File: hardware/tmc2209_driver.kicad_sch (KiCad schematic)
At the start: 10 parts

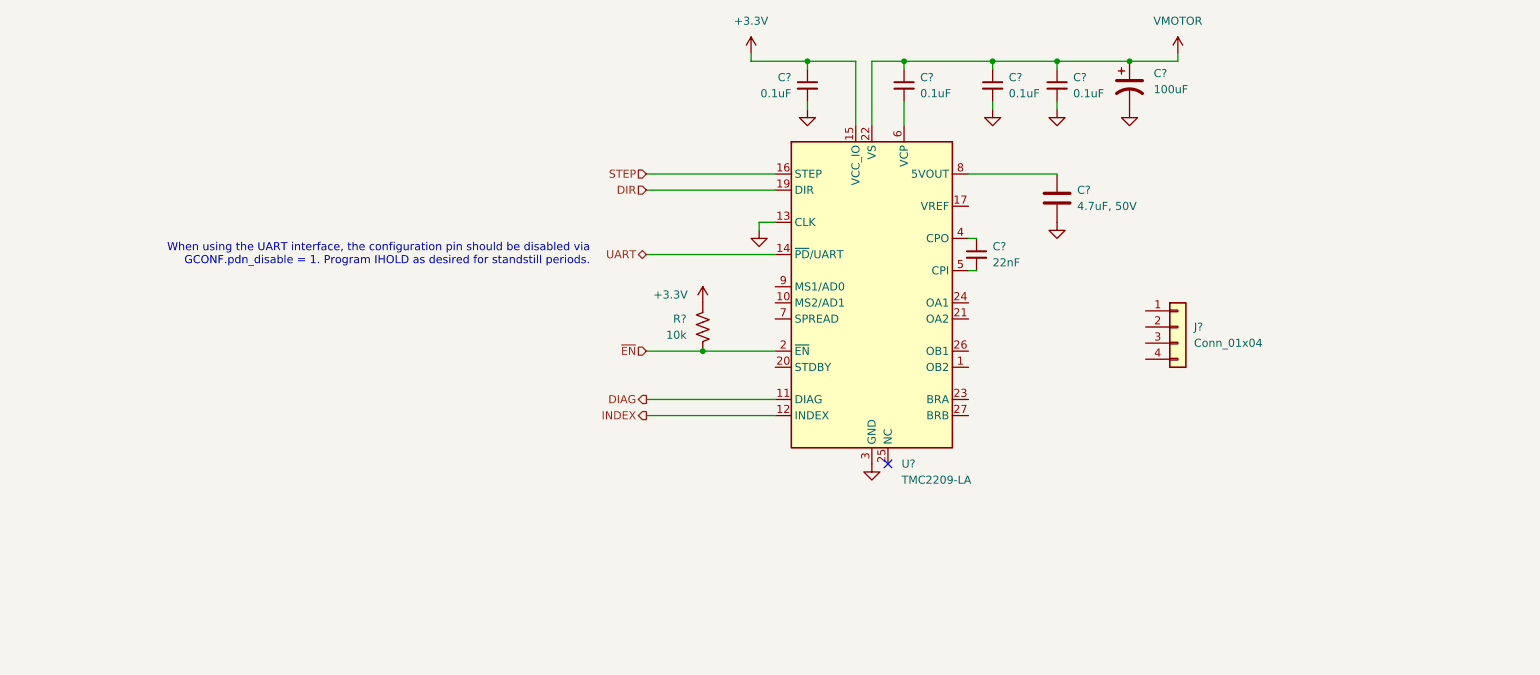
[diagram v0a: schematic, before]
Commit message: TMC2209 Schematic Improvements
Sense resistors and status LEDs
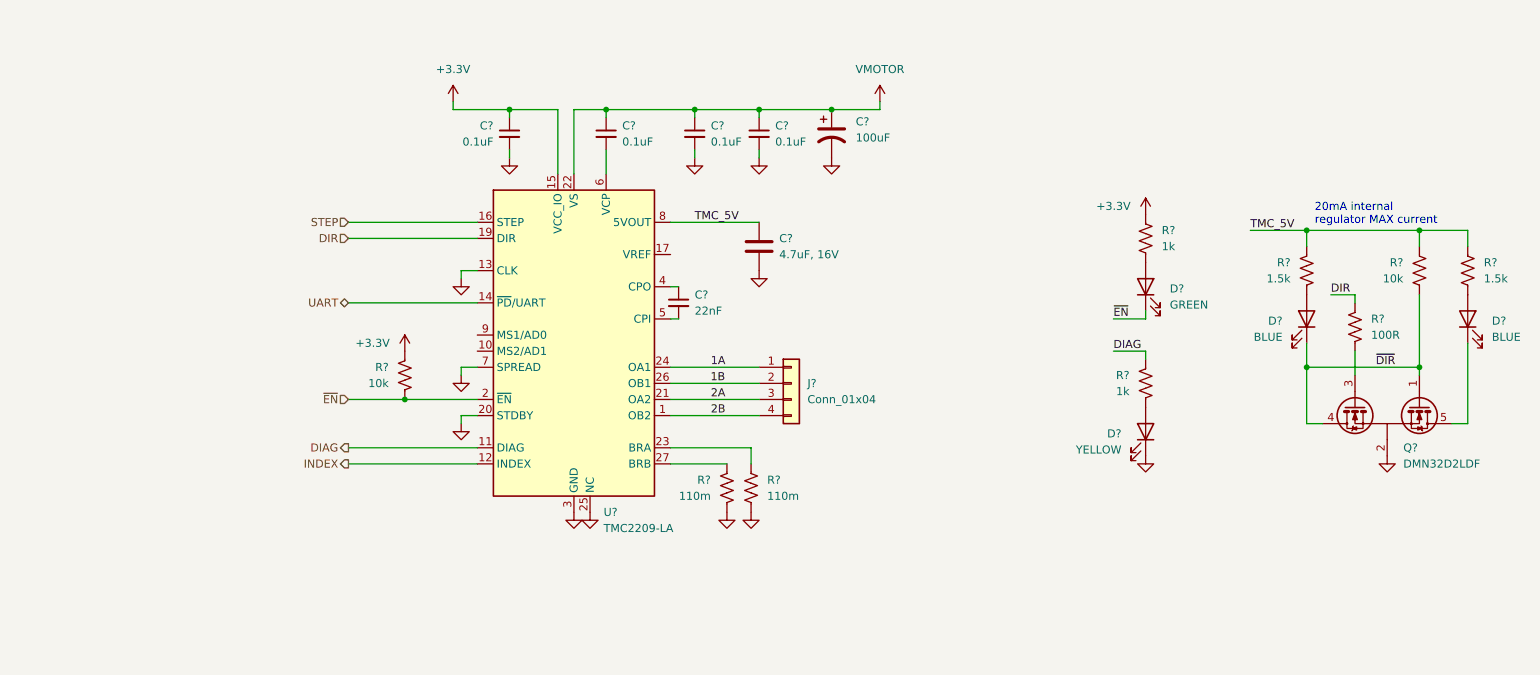
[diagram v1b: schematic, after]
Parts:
- removed C?: 4.7uF, 50V, Capacitor_SMD:C_1206_3216Metric_Pad1.33x1.80mm_HandSolder, symbol Device:C
- added C?: 4.7uF, 16V, Capacitor_SMD:C_0805_2012Metric, symbol Device:C
- added D? (x2): BLUE, Diode_SMD:D_0805_2012Metric, symbol Device:LED
- added D?: YELLOW, Diode_SMD:D_0805_2012Metric, symbol Device:LED
- added D?: GREEN, Diode_SMD:D_0805_2012Metric, symbol Device:LED
- added Q?: DMN32D2LDF, Package_TO_SOT_SMD:SOT-353_SC-70-5, symbol Transistor_FET:DMN32D2LDF
- added R? (x2): 1k, Resistor_SMD:R_0603_1608Metric, symbol Device:R_US
- added R? (x2): 1.5k, Resistor_SMD:R_0603_1608Metric, symbol Device:R_US
- added R? (x2): 110m, Resistor_SMD:R_2512_6332Metric, symbol Device:R_US
- added R?: 10k, Resistor_SMD:R_0603_1608Metric, symbol Device:R_US
- added R?: 100R, Resistor_SMD:R_0603_1608Metric, symbol Device:R_US
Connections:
- net +3.3V: now also R?.1
- net DIAG: now also R?.1
- net DIR: now also R?.1
- net GND: now also U?.20 (STDBY), U?.25 (NC), U?.7 (SPREAD), C?.2, D?.1 (K), Q?.2 (S), R?.1, R?.1
- net ~{EN}: now also D?.1 (K)
- net 2B: now reaches U?.1 (OB2)
- net 2B: now also J?.4 (Pin_4)
- net 2A: now reaches U?.21 (OA2)
- net 2A: now also J?.3 (Pin_3)
- net at U?.23 (BRA): now also R?.2
- net 1A: now reaches U?.24 (OA1)
- net 1A: now also J?.1 (Pin_1)
- net 1B: now reaches U?.26 (OB1)
- net 1B: now also J?.2 (Pin_2)
- net at U?.27 (BRB): now also R?.2
- net TMC_5V: now reaches U?.8 (5VOUT)
- net TMC_5V: now also C?.1, R?.1, R?.1, R?.1
- new net: D?.2 (A), R?.2 (x4)
- new net: D?.1 (K), Q?.5 (D1)
- new net: Q?.3 (G2), R?.2
- new net ~{DIR}: D?.1 (K), Q?.1 (G1), Q?.4 (D2), R?.2
- no-connect marks 1 -> 0
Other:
- note added: "20mA internal regulator MAX current"
- note removed: "When using the UART interface, the configuration pin should be disabled via GCONF.pdn_disable = 1. Program IHOLD as desired for standstill periods."
- moved on the sheet: C?, J?, R?, U?

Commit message: Random changes & LED additions
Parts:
- added Q?: AO3400A, Package_TO_SOT_SMD:SOT-23, symbol Transistor_FET:AO3400A
- added R?: 100R, Resistor_SMD:R_0603_1608Metric, symbol Device:R_US
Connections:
- net +3.3V: now also R?.1
- net DIAG: now also R?.1; no longer R?.1
- net GND: now also Q?.2 (S); no longer D?.1 (K)
- new net: Q?.1 (G), R?.2
- new net: D?.1 (K), Q?.3 (D)
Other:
- note added: "Connect to interrupt-capable GPIO for sensorless homing."
- note added: "DETERMINE NEED OF PULL UP/DOWN RESISTORS ON DIR AND DIAG"
- moved on the sheet: D?, Q?, R?

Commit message: Connector Updates
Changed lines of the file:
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@@
 	(text "DETERMINE NEED OF PULL UP/DOWN\nRESISTORS ON DIR AND DIAG"
 		(exclude_from_sim no)
-		(at 199.39 152.4 0)
+		(at 196.85 152.4 0)
 		(effects
 			(font

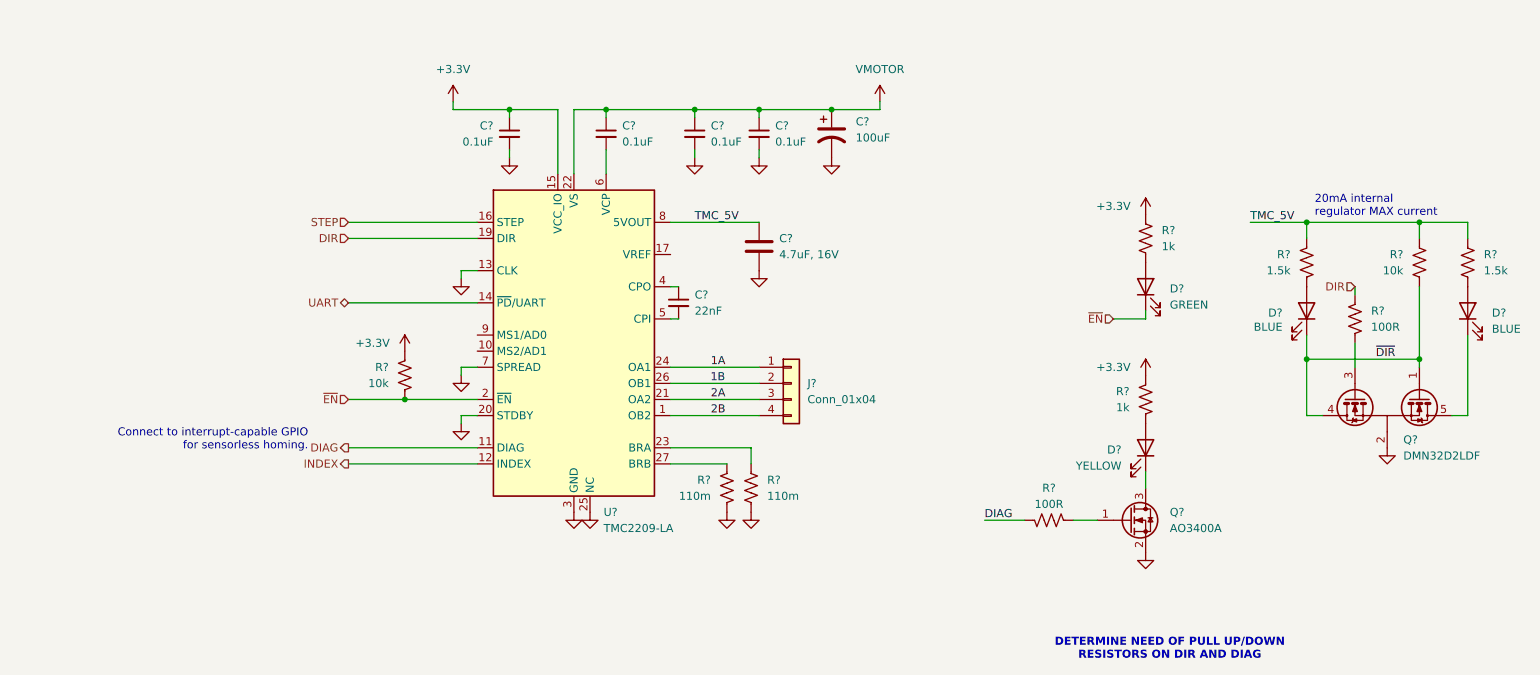
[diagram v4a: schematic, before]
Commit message: Complete TMC2209 sheet
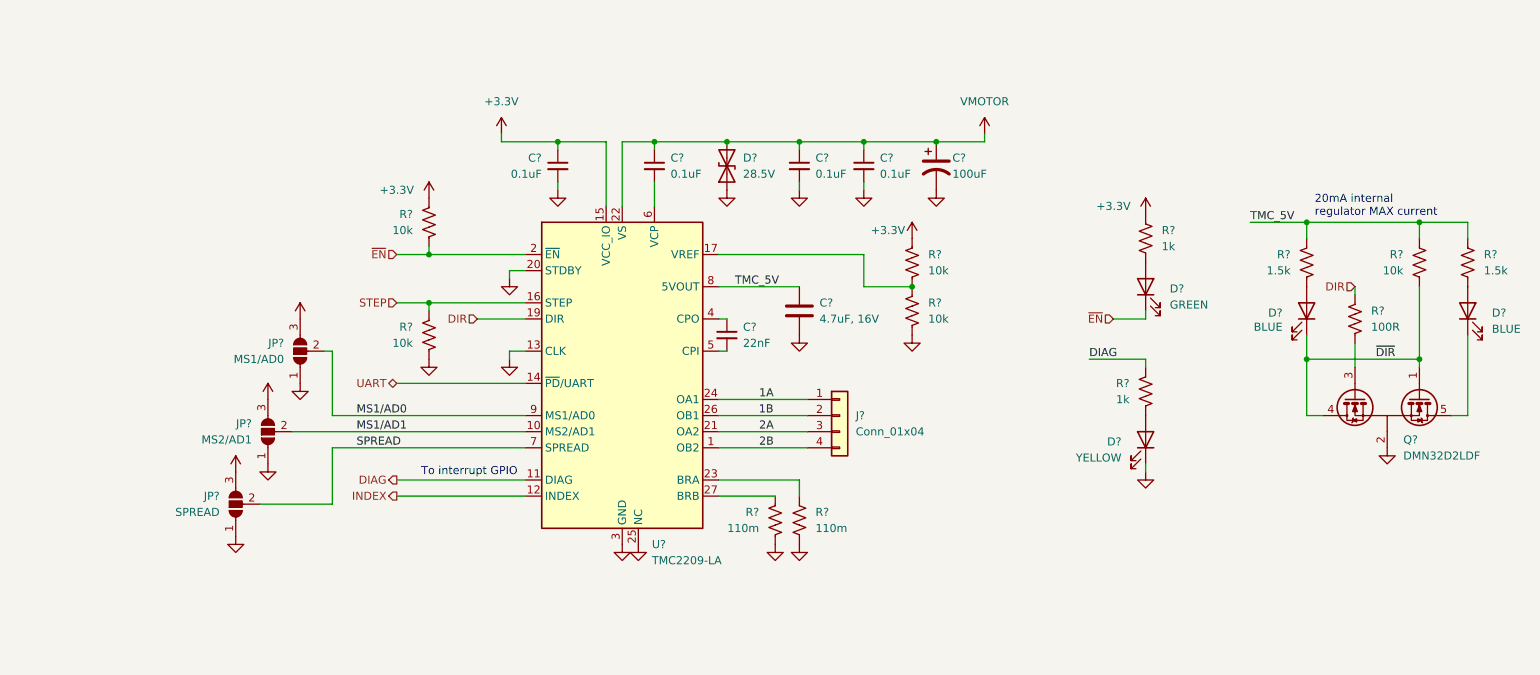
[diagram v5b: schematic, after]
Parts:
- removed D?: YELLOW, Diode_SMD:D_0805_2012Metric, symbol Device:LED
- removed Q?: AO3400A, Package_TO_SOT_SMD:SOT-23, symbol Transistor_FET:AO3400A
- removed R?: 1k, Resistor_SMD:R_0603_1608Metric, symbol Device:R_US
- removed R?: 100R, Resistor_SMD:R_0603_1608Metric, symbol Device:R_US
- added D?: 28.5V, Diode_SMD:D_SMB, symbol Device:D_TVS
- added D?: YELLOW, Diode_SMD:D_0805_2012Metric, symbol Device:LED
- added JP?: SPREAD, Jumper:SolderJumper-3_P1.3mm_Open_RoundedPad1.0x1.5mm, symbol Jumper:SolderJumper_3_Open
- added JP?: MS1/AD0, Jumper:SolderJumper-3_P1.3mm_Open_RoundedPad1.0x1.5mm, symbol Jumper:SolderJumper_3_Open
- added JP?: MS2/AD1, Jumper:SolderJumper-3_P1.3mm_Open_RoundedPad1.0x1.5mm, symbol Jumper:SolderJumper_3_Open
- added R? (x3): 10k, Resistor_SMD:R_0603_1608Metric, symbol Device:R_US
- added R?: 1k, Resistor_SMD:R_0603_1608Metric, symbol Device:R_US
- J?: Part Number (none) -> S4B-XH-A; Vendor URL (none) -> https://www.digikey.com/en/products/detail/jst-sales-americ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
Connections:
- net +3.3V: now also JP?.3 (B), JP?.3 (B), JP?.3 (B), R?.1
- net DIAG: now also R?.1
- net GND: now also D?.1 (A1), D?.1 (K), JP?.1 (A), JP?.1 (A), JP?.1 (A), R?.2, R?.2; no longer U?.7 (SPREAD)
- net STEP: now also R?.1
- net VMOTOR: now also D?.2 (A2)
- net MS1/AD1: now reaches U?.10 (MS2/AD1)
- net MS1/AD1: now also JP?.2 (C)
- net at U?.17 (VREF): now also R?.1, R?.2
- net MS1/AD0: now reaches U?.9 (MS1/AD0)
- net MS1/AD0: now also JP?.2 (C)
- new net: D?.2 (A), R?.2
- new net SPREAD: JP?.2 (C), U?.7 (SPREAD)
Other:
- note added: "To interrupt GPIO"
- note removed: "Connect to interrupt-capable GPIO for sensorless homing."
- note removed: "DETERMINE NEED OF PULL UP/DOWN RESISTORS ON DIR AND DIAG"
- company: (none) -> Jacob Wigent
- title: (none) -> Stepper Motor Driver
- moved on the sheet: C?, J?, R?, U?

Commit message: Add test points to BRA and BRB
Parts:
- added TP?: BRB, TestPoint:TestPoint_Pad_D1.0mm, symbol Connector:TestPoint_Small
- added TP?: BRA, TestPoint:TestPoint_Pad_D1.0mm, symbol Connector:TestPoint_Small
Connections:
- net at R?.2, U?.27 (BRB): now also TP?.1
- net at R?.2, U?.23 (BRA): now also TP?.1
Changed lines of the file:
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@@
 	)
 	(junction
+		(at 134.62 128.27)
+		(diameter 0)
+		(color 0 0 0 0)
+	)
+	(junction
 		(at 236.22 85.09)
 		(diameter 0)
@@
 	)
 	(junction
+		(at 138.43 125.73)
+		(diameter 0)
+		(color 0 0 0 0)
+	)
+	(junction
 		(at 148.59 72.39)
 		(diameter 0)
@@
 	)
 	(symbol
+		(lib_id "Connector:TestPoint_Small")
+		(at 134.62 128.27 0)
+		(unit 1)
+		(body_style 1)
+		(exclude_from_sim no)
+		(in_bom yes)
+		(on_board yes)
+		(in_pos_files yes)
+		(dnp no)
+		(property "Reference" "TP?"
+			(at 134.62 127 0)
+			(show_name no)
+			(do_not_autoplace no)
+			(effects
+				(font
+					(size 1.27 1.27)
+				)
+				(justify right)
+			)
+		)
+		(property "Value" "BRB"
+			(at 133.35 127 0)
+			(hide yes)
+			(show_name no)
+			(do_not_autoplace no)
+			(effects
+				(font
+					(size 1.27 1.27)
+				)
+				(justify right)
+			)
+		)
+		(property "Footprint" "TestPoint:TestPoint_Pad_D1.0mm"
+			(at 139.7 128.27 0)
+			(hide yes)
+			(show_name no)
+			(do_not_autoplace no)
+			(effects
+				(font
+					(size 1.27 1.27)
+				)
+			)
+		)
+		(property "Datasheet" ""
+			(at 139.7 128.27 0)
+			(hide yes)
+			(show_name no)
+			(do_not_autoplace no)
+			(effects
+				(font
+					(size 1.27 1.27)
+				)
+			)
+		)
+		(property "Description" "test point"
+			(at 134.62 128.27 0)
+			(hide yes)
+			(show_name no)
+			(do_not_autoplace no)
+			(effects
+				(font
+					(size 1.27 1.27)
+				)
+			)
+		)
+		(property "Part Number" ""
+			(at 134.62 128.27 0)
+			(hide yes)
+			(show_name no)
+			(do_not_autoplace no)
+			(effects
+				(font
+					(size 1.27 1.27)
+				)
+			)
+		)
+		(property "Vendor URL" ""
+			(at 134.62 128.27 0)
+			(hide yes)
+			(show_name no)
+			(do_not_autoplace no)
+			(effects
+				(font
+					(size 1.27 1.27)
+				)
+			)
+		)
+		(pin "1"
+		)
+		(instances
+			(project "stepping-stone"
+				(path "/793a882e-3f7b-468b-a863-41a1f527e1bf/3a29de04-fdfa-4d5a-abb9-c9ee2c3b40e7"
+					(reference "TP?")
+					(unit 1)
+				)
+				(path "/793a882e-3f7b-468b-a863-41a1f527e1bf/ac651d86-039a-41e0-98dc-6df0515c0885"
+					(reference "TP?")
+					(unit 1)
+				)
+				(path "/793a882e-3f7b-468b-a863-41a1f527e1bf/d8875dcc-880f-4ab2-99dc-5b365f2843f9"
+					(reference "TP?")
+					(unit 1)
+				)
+				(path "/793a882e-3f7b-468b-a863-41a1f527e1bf/e131c06c-af1f-40aa-aaad-aefd9f9dd628"
+					(reference "TP?")
+					(unit 1)
+				)
+			)
+		)
+	)
+	(symbol
 		(lib_id "power:+3.3V")
 		(at 54.61 113.03 0)
@@
 					(unit 1)
 				)
+			)
+		)
+	)
+	(symbol
+		(lib_id "Connector:TestPoint_Small")
+		(at 138.43 125.73 0)
+		(unit 1)
+		(body_style 1)
+		(exclude_from_sim no)
+		(in_bom yes)
+		(on_board yes)
+		(in_pos_files yes)
+		(dnp no)
+		(property "Reference" "TP?"
+			(at 138.43 124.46 0)
+			(show_name no)
+			(do_not_autoplace no)
+			(effects
+				(font
+					(size 1.27 1.27)
+				)
+				(justify right)
+			)
+		)
+		(property "Value" "BRA"
+			(at 139.7 126.9999 0)
+			(hide yes)
+			(show_name no)
+			(do_not_autoplace no)
+			(effects
+				(font
+					(size 1.27 1.27)
+				)
+				(justify left)
+			)
+		)
+		(property "Footprint" "TestPoint:TestPoint_Pad_D1.0mm"
+			(at 143.51 125.73 0)
+			(hide yes)
+			(show_name no)
+			(do_not_autoplace no)
+			(effects
+				(font
+					(size 1.27 1.27)
+				)
+			)
+		)
+		(property "Datasheet" ""
+			(at 143.51 125.73 0)
+			(hide yes)
+			(show_name no)
+			(do_not_autoplace no)
+			(effects
+				(font
+					(size 1.27 1.27)
+				)
+			)
+		)
+		(property "Description" "test point"
+			(at 138.43 125.73 0)
+			(hide yes)
+			(show_name no)
+			(do_not_autoplace no)
+			(effects
+				(font
+					(size 1.27 1.27)
+				)
+			)
+		)
+		(property "Part Number" ""
+			(at 138.43 125.73 0)
+			(hide yes)
+			(show_name no)
+			(do_not_autoplace no)
+			(effects
+				(font
+					(size 1.27 1.27)
+				)
+			)
+		)
+		(property "Vendor URL" ""
+			(at 138.43 125.73 0)
+			(hide yes)
+			(show_name no)
+			(do_not_autoplace no)
+			(effects
+				(font
+					(size 1.27 1.27)
+				)
+			)
+		)
+		(pin "1"
+		)
+		(instances
+			(project "stepping-stone"
+				(path "/793a882e-3f7b-468b-a863-41a1f527e1bf/3a29de04-fdfa-4d5a-abb9-c9ee2c3b40e7"
+					(reference "TP?")
+					(unit 1)
+				)
+				(path "/793a882e-3f7b-468b-a863-41a1f527e1bf/ac651d86-039a-41e0-98dc-6df0515c0885"
+					(reference "TP?")
+					(unit 1)
+				)
+				(path "/793a882e-3f7b-468b-a863-41a1f527e1bf/d8875dcc-880f-4ab2-99dc-5b365f2843f9"
+					(reference "TP?")
+					(unit 1)
+				)
+				(path "/793a882e-3f7b-468b-a863-41a1f527e1bf/e131c06c-af1f-40aa-aaad-aefd9f9dd628"
+					(reference "TP?")
+					(unit 1)
+				)

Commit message: SD Card Pull Ups and ESD
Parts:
- added JP?: VREF, Jumper:SolderJumper-2_P1.3mm_Bridged_RoundedPad1.0x1.5mm, symbol Jumper:SolderJumper_2_Bridged
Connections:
- net at R?.1, R?.2: now also JP?.2 (B); no longer U?.17 (VREF)
- new net: JP?.1 (A), U?.17 (VREF)
